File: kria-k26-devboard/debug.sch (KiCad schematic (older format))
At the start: 70 parts, among them J8 USB4105-GF-A, J9 0878311420, Q10 BSS138-7-F, Q11 BSS138-7-F, Q17 DTC014TEBTL, Q9 BSS138-7-F, U29 MIC5211-3.3YM6-TR, U30 FT4232HPQ, U31 93LC56CT-IMC, U32 74AVC4T245RSVRG4, U33 74AVC4T245RSVRG4, U34 SN74AVC2T245RSWR, U35 SN74AVC2T245RSWR, U36 NC7WZ07P6X, Y5 ABM8G-12.000MHZ-18-D2Y-T

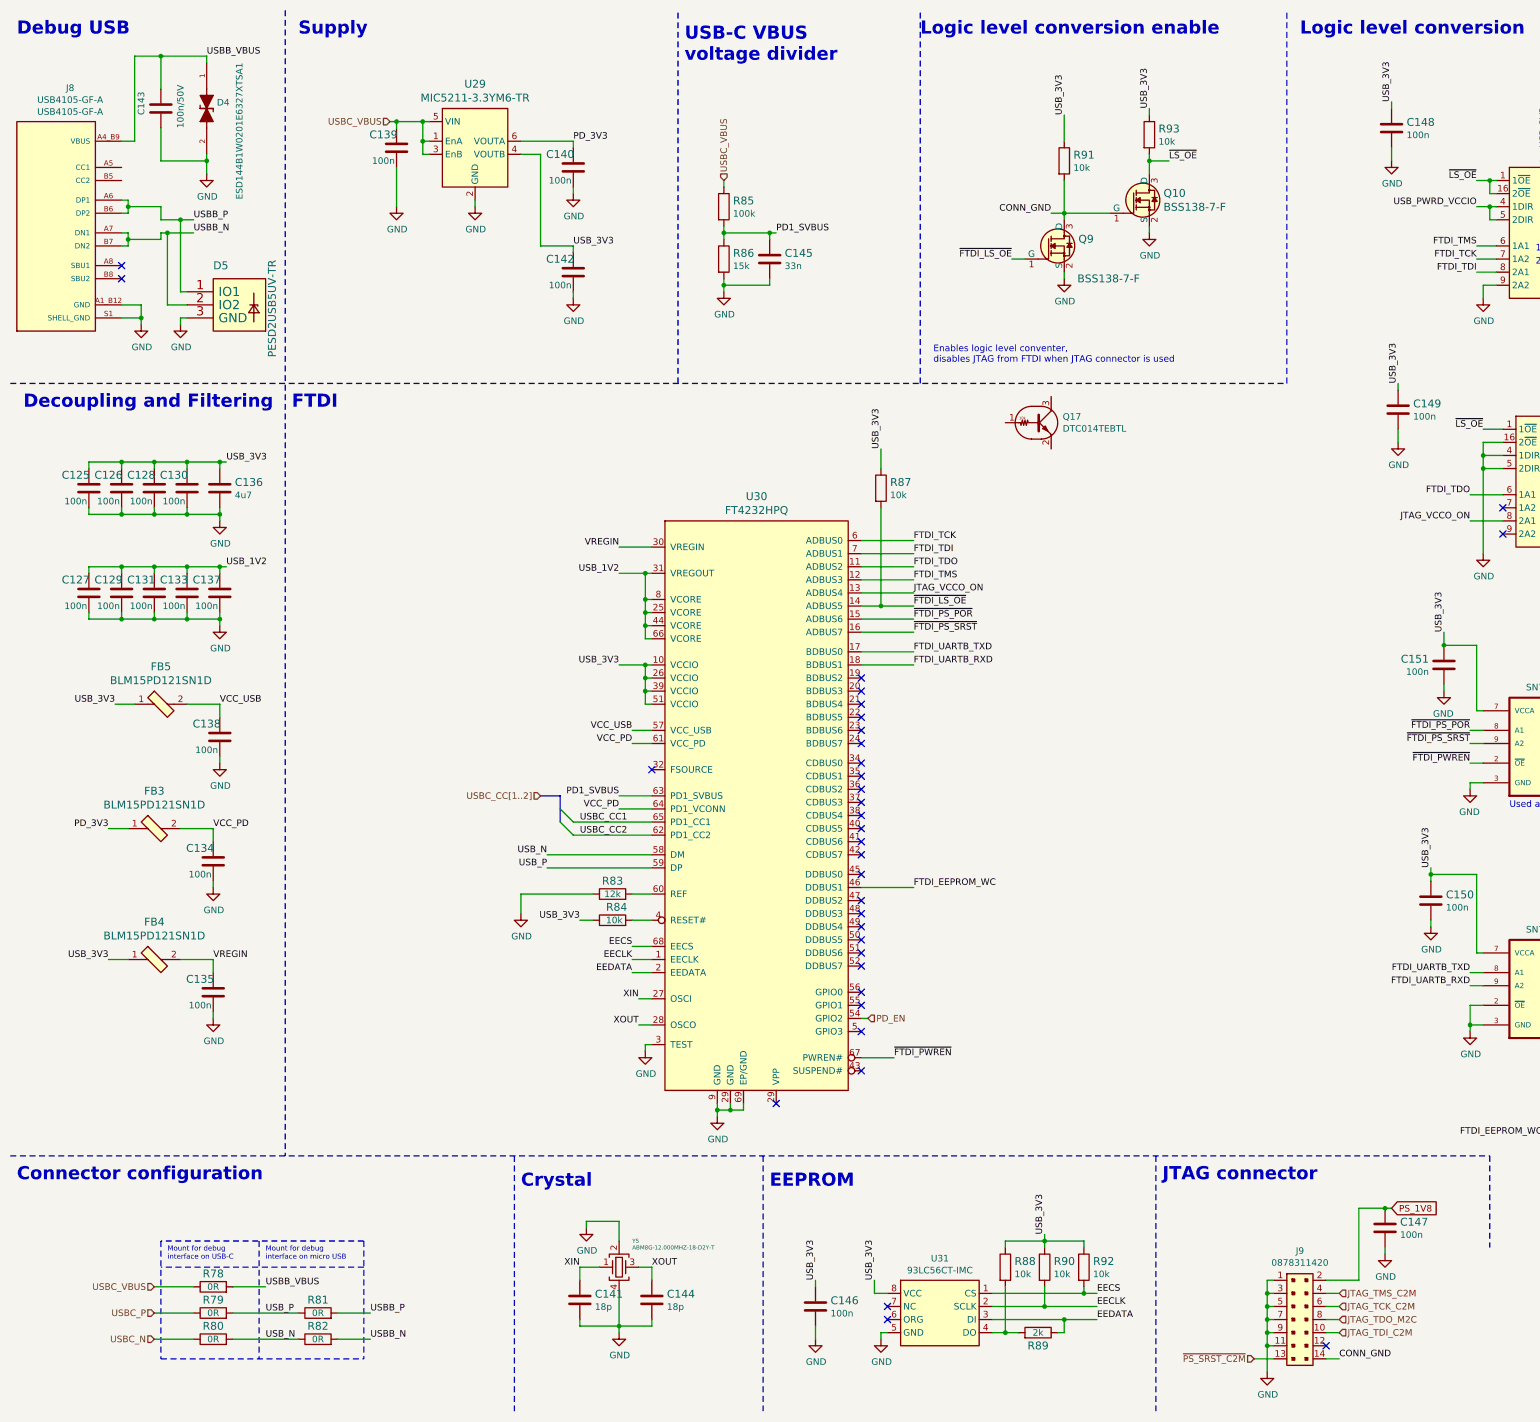
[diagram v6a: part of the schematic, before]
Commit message: Routed I2C, JTAG, PS reset, remaining differential pairs. Component optimization
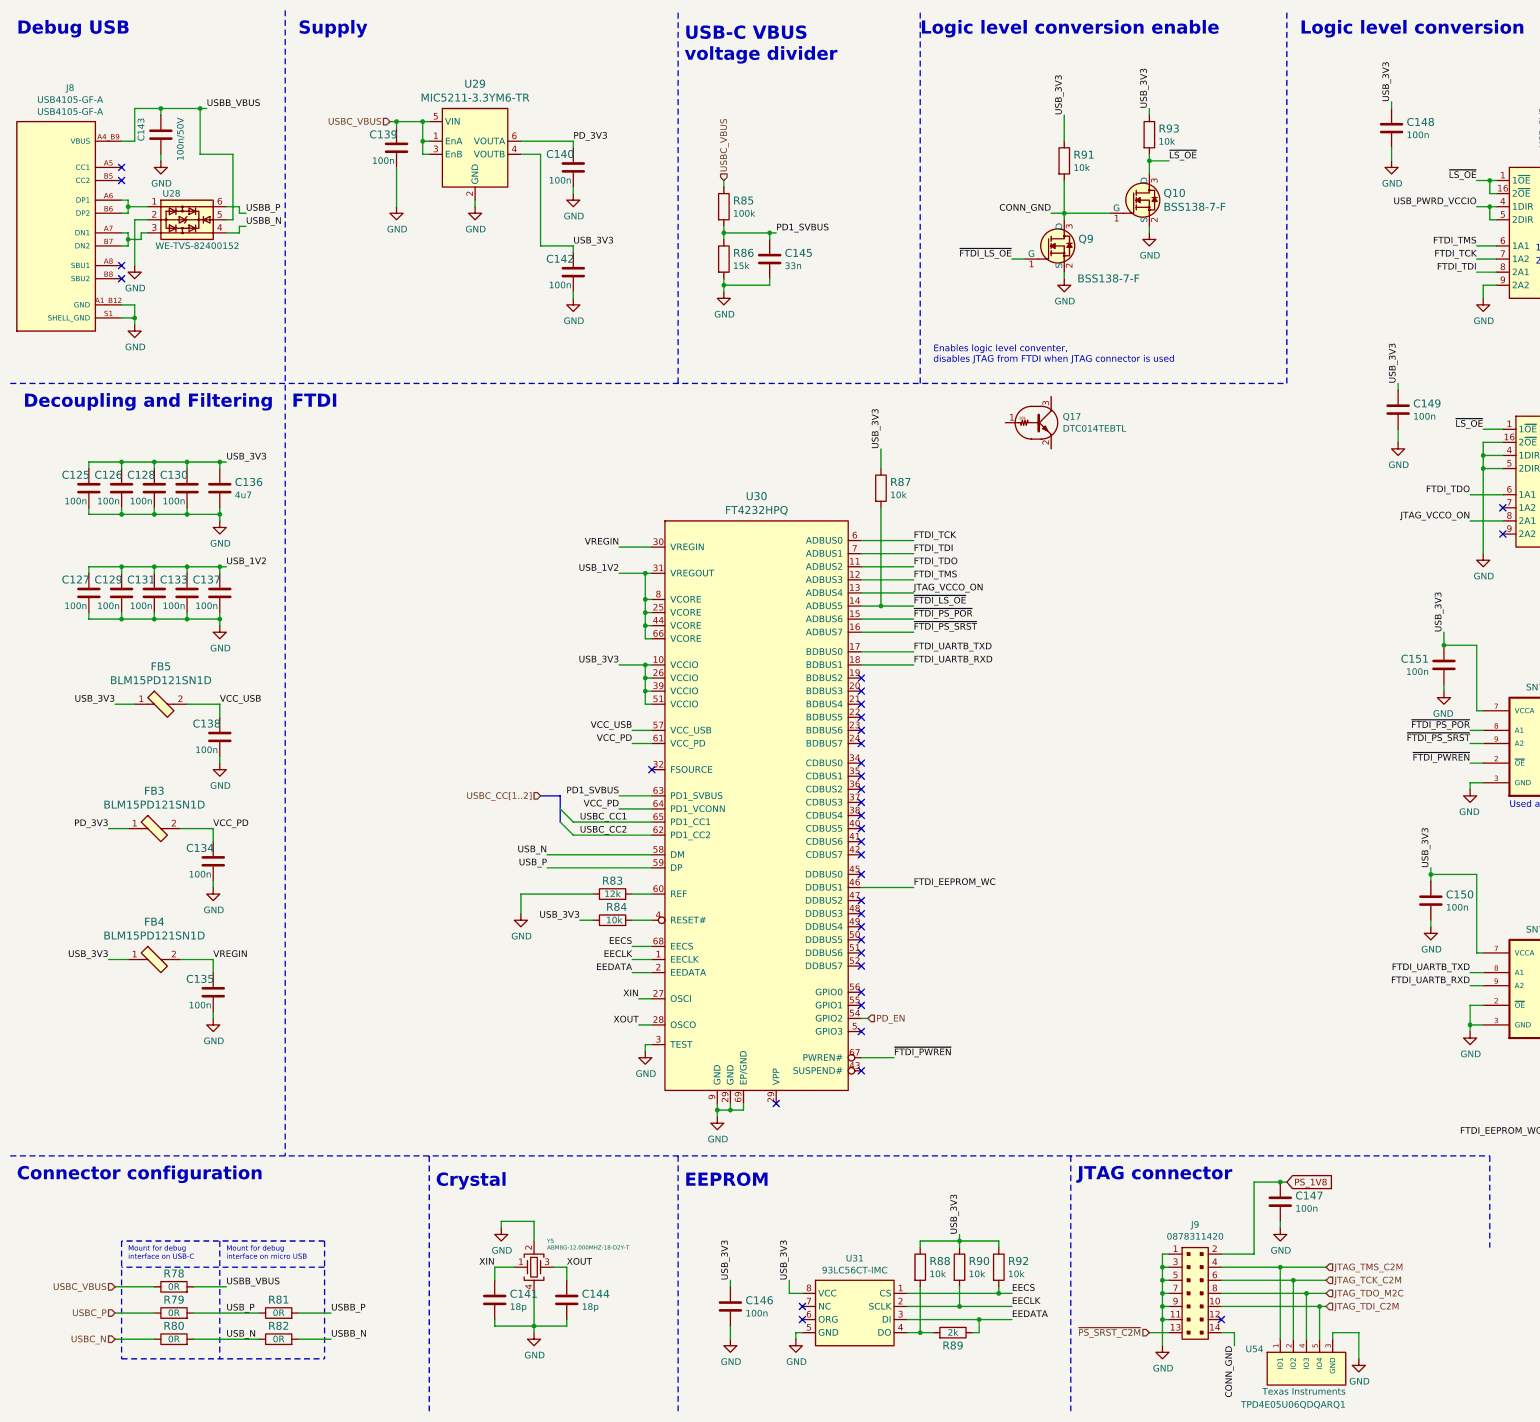
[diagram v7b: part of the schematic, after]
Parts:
- removed D4: ESD144B1W0201E6327XTSA1, antmicro-footprints:ESD144B1W0201E6327XTSA1, symbol antmicroTVSDiodes:ESD144B1W0201E6327XTSA1
- removed D5: PESD2USB5UV-TR, antmicro-footprints:SOT-23s, symbol antmicroTVSDiodes:PESD2USB5UV-TR
- added U28: WE-TVS-82400152, antmicro-footprints:SOT-563, symbol antmicroTVSDiodes:WE-TVS-82400152
- added U54: TPD4E05U06QDQARQ1, antmicro-footprints:TPD4E05U06QDQARQ1, symbol antmicroTVSDiodes:TPD4E05U06QDQARQ1
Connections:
- net GND: now also U28.2, U54.3 (GND), U54.8 (GND)
- net JTAG_TCK_C2M: now also U54.2 (IO2), U54.9 (IO2)
- net JTAG_TDI_C2M: now also U54.5 (IO4), U54.6 (IO4)
- net JTAG_TDO_M2C: now also U54.4 (IO3), U54.7 (IO3)
- net JTAG_TMS_C2M: now also U54.1 (IO1), U54.10 (IO1)
- net USBB_N: now also U28.4; no longer J8.A7 (DN1), J8.B7 (DN2)
- net USBB_P: now also U28.6; no longer J8.A6 (DP1), J8.B6 (DP2)
- net VBUS: now also U28.5
- new net: J8.A6 (DP1), J8.B6 (DP2), U28.1
- new net: J8.A7 (DN1), J8.B7 (DN2), U28.3
- no-connect marks 35 -> 37
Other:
- moved on the sheet: C141, C143, C144, C146, C147, J9, R78, R79, R80, R81, R82, R88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
